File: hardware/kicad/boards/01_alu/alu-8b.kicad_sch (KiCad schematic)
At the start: 16 parts

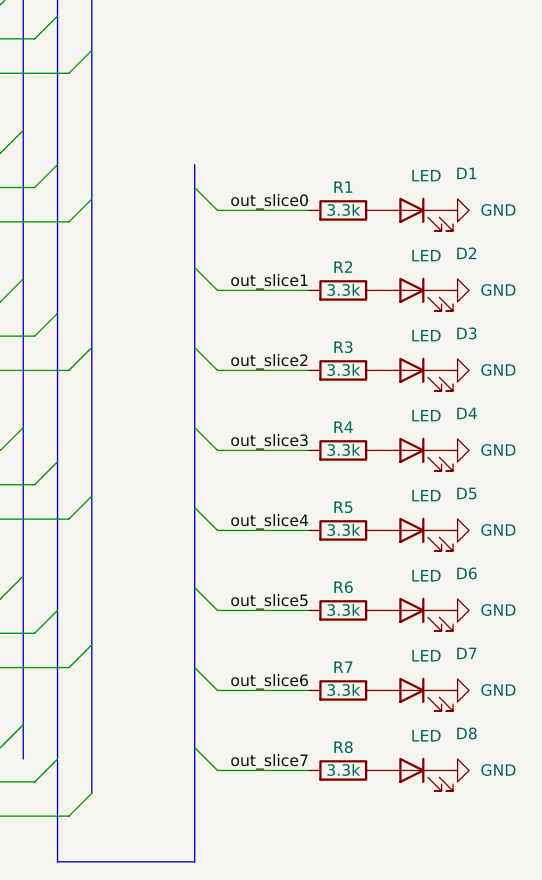
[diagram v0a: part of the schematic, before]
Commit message: feat: designed ALU board with 0 ERC errors or warnings 🎉
Final review of logical correctness and footprints and then routing begins
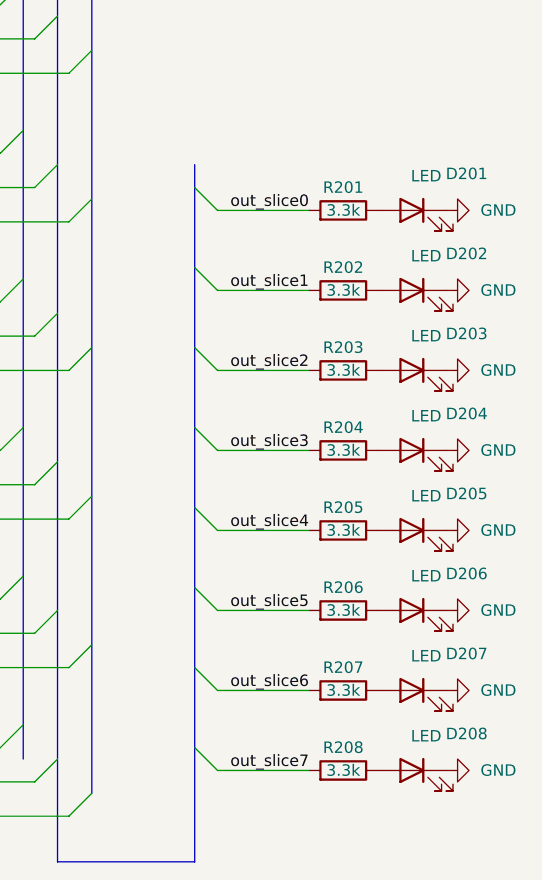
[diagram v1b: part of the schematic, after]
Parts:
- renumbered D1 to D201, D2 to D202, D3 to D203, D4 to D204, D5 to D205, D6 to D206, D7 to D207, D8 to D208, R1 to R201, R2 to R202, R3 to R203, R4 to R204, R5 to R205, R6 to R206, R7 to R207, R8 to R208

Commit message: arch: added LEDs, override switches; fixed errors and warnings to 0
ready for routing after logical coherence check
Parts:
- removed D201, D202, D203, D204, D205, D206, D207, D208: LED, LED_THT:LED_D5.0mm, symbol Device:LED
- removed R201, R202, R203, R204, R205, R206, R207, R208: 3.3k, Resistor_SMD:R_0805_2012Metric, symbol Device:R

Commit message: schematics: designed alu into 4b slices saving several chips and "de-bloating" board of several glue and drivers
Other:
- sheet alu-1b-0 ports: added ~G, ~P; removed G, P
- sheet alu-1b-1 ports: added ~G, ~P; removed G, P
- sheet alu-1b-2 ports: added ~G, ~P; removed G, P
- sheet alu-1b-3 ports: added ~G, ~P; removed G, P
- sheet alu-1b-4 ports: added ~G, ~P; removed G, P
- sheet alu-1b-5 ports: added ~G, ~P; removed G, P
- sheet alu-1b-6 ports: added ~G, ~P; removed G, P
- sheet alu-1b-7 ports: added ~G, ~P; removed G, P
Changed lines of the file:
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@@
-			)
-		)
-		(pin "P" output
-			(at 62.23 55.88 0)
-			(effects
-				(font
-					(size 1.27 1.27)
-				)
-				(justify right)
-			)
-		)
-		(pin "G" output
-			(at 62.23 63.5 0)
-			(effects
-				(font
-					(size 1.27 1.27)
-				)
-				(justify right)
 			)
 		)
@@
 		(pin "1b-out" output
 			(at 62.23 59.69 0)
+			(effects
+				(font
+					(size 1.27 1.27)
+				)
+				(justify right)
+			)
+		)
+		(pin "~G" output
+			(at 62.23 63.5 0)
+			(effects
+				(font
+					(size 1.27 1.27)
+				)
+				(justify right)
+			)
+		)
+		(pin "~P" output
+			(at 62.23 55.88 0)
 			(effects
 				(font
@@
 			)
 		)
-		(pin "P" output
-			(at 62.23 139.7 0)
-			(effects
-				(font
-					(size 1.27 1.27)
-				)
-				(justify right)
-			)
-		)
-		(pin "G" output
-			(at 62.23 147.32 0)
-			(effects
-				(font
-					(size 1.27 1.27)
-				)
-				(justify right)
-			)
-		)
 		(pin "c" input
 			(at 49.53 147.32 180)
@@
 		(pin "1b-out" output
 			(at 62.23 143.51 0)
+			(effects
+				(font
+					(size 1.27 1.27)
+				)
+				(justify right)
+			)
+		)
+		(pin "~G" output
+			(at 62.23 147.32 0)
+			(effects
+				(font
+					(size 1.27 1.27)
+				)
+				(justify right)
+			)
+		)
+		(pin "~P" output
+			(at 62.23 139.7 0)
 			(effects
 				(font
@@
 			)
 		)
-		(pin "P" output
-			(at 62.23 123.19 0)
-			(effects
-				(font
-					(size 1.27 1.27)
-				)
-				(justify right)
-			)
-		)
-		(pin "G" output
-			(at 62.23 130.81 0)
-			(effects
-				(font
-					(size 1.27 1.27)
-				)
-				(justify right)
-			)
-		)
 		(pin "c" input
 			(at 49.53 130.81 180)
@@
 		(pin "1b-out" output
 			(at 62.23 127 0)
+			(effects
+				(font
+					(size 1.27 1.27)
+				)
+				(justify right)
+			)
+		)
+		(pin "~G" output
+			(at 62.23 130.81 0)
+			(effects
+				(font
+					(size 1.27 1.27)
+				)
+				(justify right)
+			)
+		)
+		(pin "~P" output
+			(at 62.23 123.19 0)
 			(effects
 				(font
@@
 			)
 		)
-		(pin "P" output
-			(at 62.23 39.37 0)
-			(effects
-				(font
-					(size 1.27 1.27)
-				)
-				(justify right)
-			)
-		)
-		(pin "G" output
-			(at 62.23 46.99 0)
-			(effects
-				(font
-					(size 1.27 1.27)
-				)
-				(justify right)
-			)
-		)
 		(pin "c" input
 			(at 49.53 46.99 180)
@@
 		(pin "1b-out" output
 			(at 62.23 43.18 0)
+			(effects
+				(font
+					(size 1.27 1.27)
+				)
+				(justify right)
+			)
+		)
+		(pin "~G" output
+			(at 62.23 46.99 0)
+			(effects
+				(font
+					(size 1.27 1.27)
+				)
+				(justify right)
+			)
+		)
+		(pin "~P" output
+			(at 62.23 39.37 0)
 			(effects
 				(font
@@
 			)
 		)
-		(pin "P" output
-			(at 62.23 73.66 0)
-			(effects
-				(font
-					(size 1.27 1.27)
-				)
-				(justify right)
-			)
-		)
-		(pin "G" output
-			(at 62.23 81.28 0)
-			(effects
-				(font
-					(size 1.27 1.27)
-				)
-				(justify right)
-			)
-		)
 		(pin "c" input
 			(at 49.53 81.28 180)
@@
 		(pin "1b-out" output
 			(at 62.23 77.47 0)
+			(effects
+				(font
+					(size 1.27 1.27)
+				)
+				(justify right)
+			)
+		)
+		(pin "~G" output
+			(at 62.23 81.28 0)
+			(effects
+				(font
+					(size 1.27 1.27)
+				)
+				(justify right)
+			)
+		)
+		(pin "~P" output
+			(at 62.23 73.66 0)
 			(effects
 				(font
@@
 			)
 		)
-		(pin "P" output
-			(at 62.23 156.21 0)
-			(effects
-				(font
-					(size 1.27 1.27)
-				)
-				(justify right)
-			)
-		)
-		(pin "G" output
-			(at 62.23 163.83 0)
-			(effects
-				(font
-					(size 1.27 1.27)
-				)
-				(justify right)
-			)
-		)
 		(pin "c" input
 			(at 49.53 163.83 180)
@@
 		(pin "1b-out" output
 			(at 62.23 160.02 0)
+			(effects
+				(font
+					(size 1.27 1.27)
+				)
+				(justify right)
+			)
+		)
+		(pin "~G" output
+			(at 62.23 163.83 0)
+			(effects
+				(font
+					(size 1.27 1.27)
+				)
+				(justify right)
+			)
+		)
+		(pin "~P" output
+			(at 62.23 156.21 0)
 			(effects
 				(font
@@
 			)
 		)
-		(pin "P" output
-			(at 62.23 106.68 0)
-			(effects
-				(font
-					(size 1.27 1.27)
-				)
-				(justify right)
-			)
-		)
 		(pin "c" input
 			(at 49.53 114.3 180)
@@
 			)
 		)
-		(pin "G" output
+		(pin "~G" output
 			(at 62.23 114.3 0)
+			(effects
+				(font
+					(size 1.27 1.27)
+				)
+				(justify right)
+			)
+		)
+		(pin "~P" output
+			(at 62.23 106.68 0)
 			(effects
 				(font
@@
 			)
 		)
-		(pin "P" output
-			(at 62.23 90.17 0)
-			(effects
-				(font
-					(size 1.27 1.27)
-				)
-				(justify right)
-			)
-		)
-		(pin "G" output
-			(at 62.23 97.79 0)
-			(effects
-				(font
-					(size 1.27 1.27)
-				)
-				(justify right)
-			)
-		)
 		(pin "c" input
 			(at 49.53 97.79 180)
@@
 			(effects
 				(font
+					(size 1.27 1.27)
+				)
+				(justify right)
+			)
+		)
+		(pin "~G" output
+			(at 62.23 97.79 0)
+			(effects
+				(font
+					(size 1.27 1.27)
+				)
+				(justify right)
+			)
+		)
+		(pin "~P" output
+			(at 62.23 90.17 0)
+			(effects
+				(font
